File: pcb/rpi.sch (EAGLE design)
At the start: 32 parts, among them IC1 LD117AS33TR, SW1 324_SW, SW20 324_SW, U5 CH340C

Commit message: rpi carrier board finished
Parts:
- removed C14, C15, C17, C19, C35: 100nF, clock:CAP0805
- removed C18: 1uF, clock:CAP0805
- removed U$2, U$3, U$4, U$5: M2.5HOLE, f1c100s:M2.5HOLE
- added JP3, JP4, JP5: (no value), pinhead:PINHD-1X3
- added R2, R3: 390K, SparkFun-Passives:RESISTOR0805-RES
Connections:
- removed net N$17: SW20.2, SW20.3
- removed net N$4: SW1.2, SW1.3
- new net N$11: JP1.15, JP2.15, PCB1.GPIO22, R3.1, SW20.2, SW20.3
- new net N$12: JP1.19, JP2.19, PCB1.GPIO10, U2.SDIN
- new net N$13: JP1.21, JP2.21, PCB1.GPIO9
- new net N$14: JP1.23, JP2.23, PCB1.GPIO11, U2.SCLK
- new net N$15: JP1.27, JP2.27, PCB1.ID_SD*
- new net N$16: JP1.29, JP2.29, PCB1.GPIO5, U2.DC
- new net N$19: JP1.33, JP2.33, PCB1.GPIO13
- new net N$20: JP1.35, JP2.35, PCB1.GPIO19
- new net N$21: JP1.37, JP2.37, PCB1.GPIO26
- new net N$22: JP1.12, JP2.12, PCB1.GPIO18
- new net N$23: JP1.16, JP2.16, PCB1.GPIO23
- new net N$24: JP1.18, JP2.18, PCB1.GPIO24
- new net N$25: JP1.22, JP2.22, PCB1.GPIO25
- new net N$26: JP1.24, JP2.24, PCB1.GPIO8
- new net N$27: JP1.26, JP2.26, PCB1.GPIO7, U2./CS
- new net N$28: JP1.28, JP2.28, PCB1.ID_SC*
- new net N$29: JP1.32, JP2.32, PCB1.GPIO12
- new net N$30: JP1.36, JP2.36, PCB1.GPIO16
- new net N$31: JP1.38, JP2.38, PCB1.GPIO20
- new net N$32: JP1.40, JP2.40, PCB1.GPIO21
- new net N$34: JP1.13, JP2.13, PCB1.GPIO27, R2.1, SW1.2, SW1.3
- new net N$5: JP1.3, JP2.3, PCB1.GPIO2
- new net N$6: JP1.5, JP2.5, PCB1.GPIO3
- new net N$8: JP1.7, JP2.7, PCB1.GPIO4
- new net N$9: JP1.11, JP2.11, PCB1.GPIO17
- net +3V3: now also JP2.17, JP3.1, JP3.2, JP3.3, R2.2, R3.2; no longer C14.2, C15.2, C17.2, C18.2, C19.2, C35.2
- net +5V: now also JP5.1, JP5.2, JP5.3
- net GND: now also JP4.1, JP4.2, JP4.3; no longer C14.1, C15.1, C17.1, C18.1, C19.1, C35.1
- net N$43: now also JP1.31, JP2.31, PCB1.GPIO6
- net UART0_RX: now also JP1.10, JP2.10
- net UART0_TX: now also JP1.8, JP2.8
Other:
- moved on the sheet: C20, C21, C22, C23, JP1, R7, R8, U2

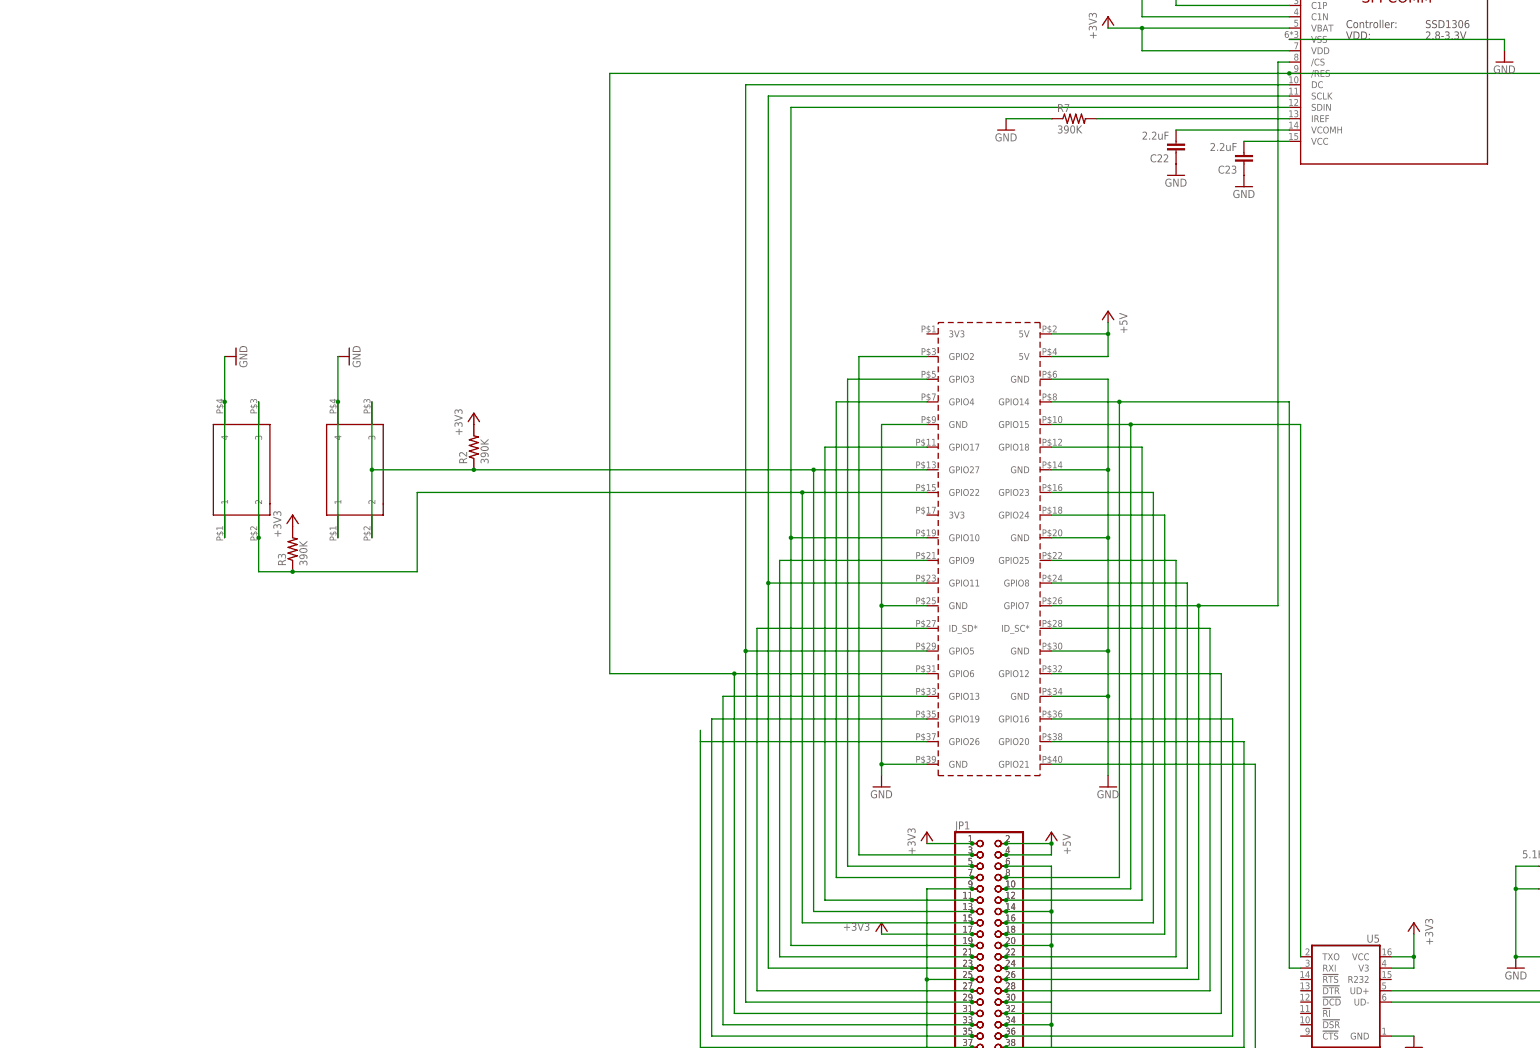
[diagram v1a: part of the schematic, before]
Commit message: updated baseboard, added power buttons
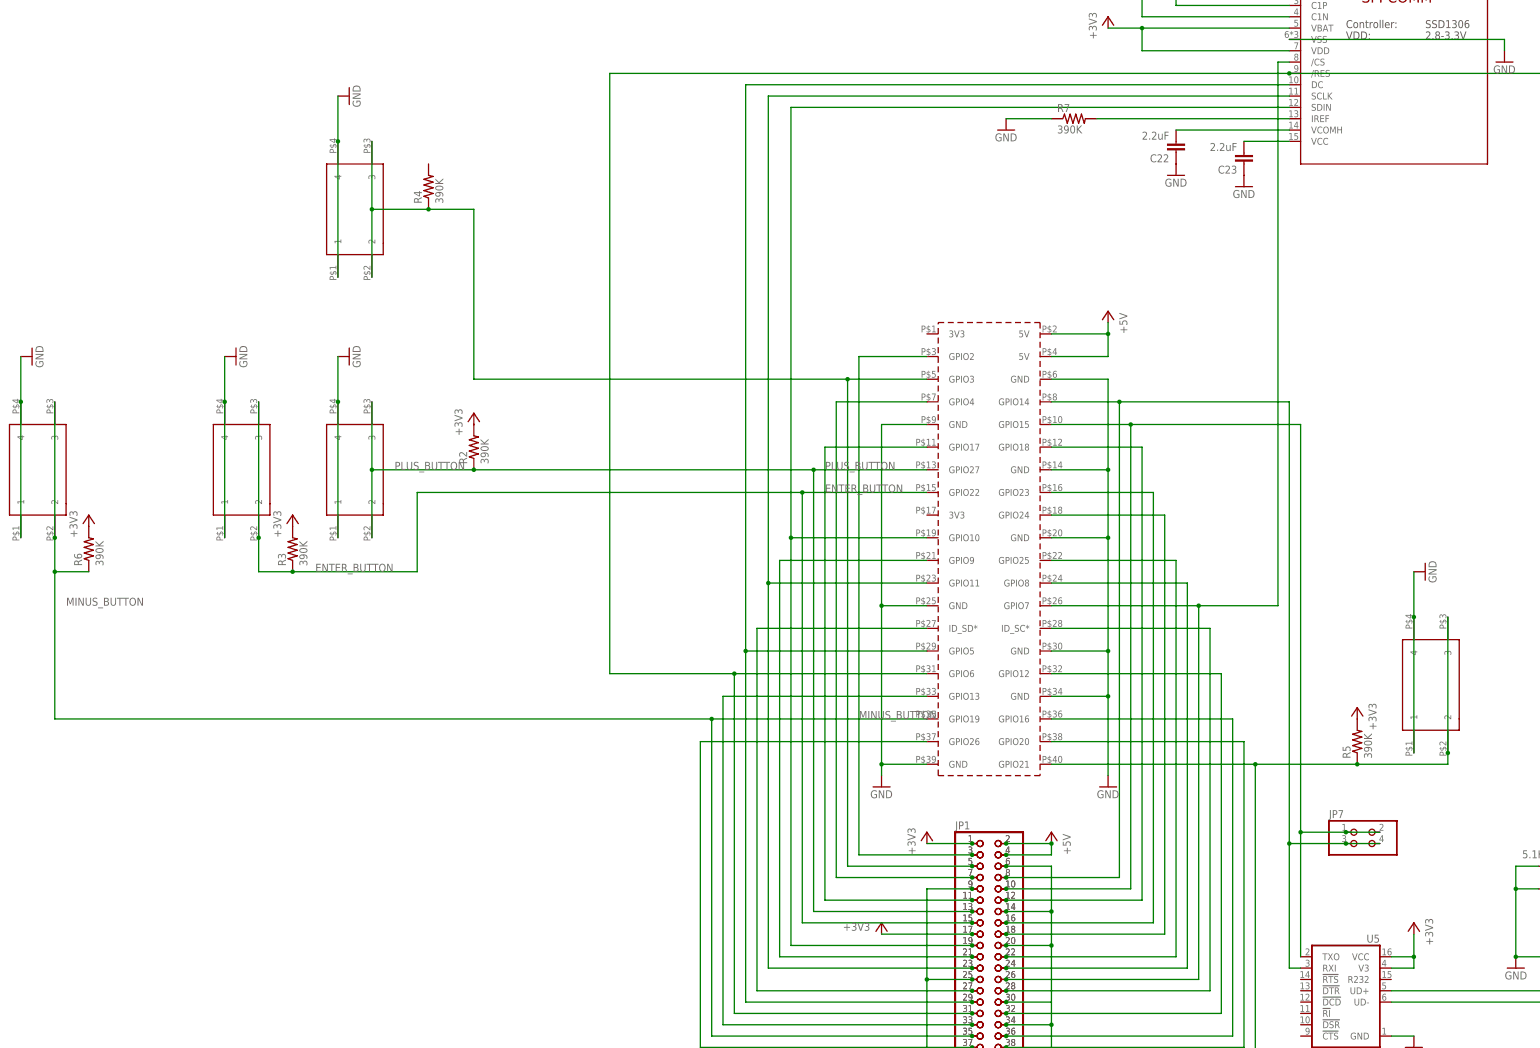
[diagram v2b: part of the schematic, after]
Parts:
- added JP7: (no value), pinhead:PINHD-2X2
- added R4, R5, R6: 390K, SparkFun-Passives:RESISTOR0805-RES
- added SW2, SW3, SW4: 324_SW, 3pos_slide_switch_centered:324_SW
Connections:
- net N$11 renamed ENTER_BUTTON
- net N$34 renamed PLUS_BUTTON
- removed net N$20: JP1.35, JP2.35, PCB1.GPIO19
- removed net UART0_RX: JP1.10, JP2.10, PCB1.GPIO15, U5.TXO
- removed net UART0_TX: JP1.8, JP2.8, PCB1.GPIO14, U5.RXI
- new net MINUS_BUTTON: JP1.35, JP2.35, PCB1.GPIO19, R6.1, SW4.2, SW4.3
- new net RPI_RX: JP1.10, JP2.10, JP7.1, JP7.2, PCB1.GPIO15, U5.TXO
- new net RPI_TX: JP1.8, JP2.8, JP7.3, JP7.4, PCB1.GPIO14, U5.RXI
- net +3V3: now also R5.2, R6.2
- net GND: now also SW2.1, SW2.4, SW3.1, SW3.4, SW4.1, SW4.4
- net N$32: now also R5.1, SW3.2, SW3.3
- net N$6: now also R4.1, SW2.2, SW2.3

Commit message: added i2c pullups, cleanup
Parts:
- removed R4: 390K, SparkFun-Passives:RESISTOR0805-RES
- added R10, R11: 5.1K, joyAnalog:RESISTOR0805-RES
- added U$2, U$3: M2.5HOLE, f1c100s:M2.5HOLE
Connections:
- net +3V3: now also R10.1, R11.1
- net N$5: now also R11.2
- net N$6: now also R10.2; no longer R4.1
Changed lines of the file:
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@@
 <layer number="250" name="Descript" color="3" fill="1" visible="no" active="no"/>
 <layer number="251" name="SMDround" color="12" fill="11" visible="no" active="no"/>
+<layer number="253" name="Extra" color="7" fill="1" visible="no" active="no"/>
 <layer number="254" name="cooling" color="7" fill="1" visible="yes" active="yes"/>
 <layer number="255" name="routoute" color="7" fill="1" visible="yes" active="yes"/>
@@
 <part name="SW3" library="3pos_slide_switch_centered" deviceset="324_SW" device="" value="324_SW"/>
 <part name="GND9" library="supply1" library_urn="urn:adsk.eagle:library:371" deviceset="GND" device=""/>
-<part name="R4" library="SparkFun-Passives" deviceset="RESISTOR" device="0805-RES" value="390K"/>
 <part name="R5" library="SparkFun-Passives" deviceset="RESISTOR" device="0805-RES" value="390K"/>
 <part name="+3V7" library="supply1" library_urn="urn:adsk.eagle:library:371" deviceset="+3V3" device=""/>
@@
 <part name="R6" library="SparkFun-Passives" deviceset="RESISTOR" device="0805-RES" value="390K"/>
 <part name="+3V8" library="supply1" library_urn="urn:adsk.eagle:library:371" deviceset="+3V3" device=""/>
+<part name="R10" library="joyAnalog" deviceset="RESISTOR" device="0805-RES" value="5.1K"/>
+<part name="R11" library="joyAnalog" deviceset="RESISTOR" device="0805-RES" value="5.1K"/>
+<part name="+3V9" library="supply1" library_urn="urn:adsk.eagle:library:371" deviceset="+3V3" device=""/>
+<part name="+3V12" library="supply1" library_urn="urn:adsk.eagle:library:371" deviceset="+3V3" device=""/>
+<part name="U$2" library="f1c100s" deviceset="M2.5HOLE" device=""/>
+<part name="U$3" library="f1c100s" deviceset="M2.5HOLE" device=""/>
 </parts>
 <sheets>
@@
 <attribute name="VALUE" x="739.14" y="40.64" size="1.778" layer="96" rot="R90"/>
 </instance>
-<instance part="R4" gate="G$1" x="513.08" y="129.54" smashed="yes" rot="R90">
-<attribute name="NAME" x="511.5814" y="125.73" size="1.778" layer="95" rot="R90"/>
-<attribute name="VALUE" x="516.382" y="125.73" size="1.778" layer="96" rot="R90"/>
-</instance>
 <instance part="R5" gate="G$1" x="721.36" y="5.08" smashed="yes" rot="R90">
 <attribute name="NAME" x="719.8614" y="1.27" size="1.778" layer="95" rot="R90"/>
@@
 <attribute name="VALUE" x="434.34" y="50.8" size="1.778" layer="96" rot="R90"/>
 </instance>
+<instance part="R10" gate="G$1" x="645.16" y="111.76" smashed="yes" rot="MR270">
+<attribute name="NAME" x="643.6614" y="113.03" size="1.778" layer="95" rot="MR270"/>
+<attribute name="VALUE" x="643.382" y="107.95" size="1.778" layer="96" rot="MR270"/>
+</instance>
+<instance part="R11" gate="G$1" x="632.46" y="111.76" smashed="yes" rot="MR270">
+<attribute name="NAME" x="630.9614" y="113.03" size="1.778" layer="95" rot="MR270"/>
+<attribute name="VALUE" x="630.682" y="107.95" size="1.778" layer="96" rot="MR270"/>
+</instance>
+<instance part="+3V9" gate="G$1" x="645.16" y="124.46" smashed="yes">
+<attribute name="VALUE" x="642.62" y="119.38" size="1.778" layer="96" rot="R90"/>
+</instance>
+<instance part="+3V12" gate="G$1" x="632.46" y="124.46" smashed="yes">
+<attribute name="VALUE" x="629.92" y="119.38" size="1.778" layer="96" rot="R90"/>
+</instance>
+<instance part="U$2" gate="G$1" x="881.38" y="88.9" smashed="yes"/>
+<instance part="U$3" gate="G$1" x="881.38" y="73.66" smashed="yes"/>
 </instances>
 <busses>
@@
 <pinref part="+3V8" gate="G$1" pin="+3V3"/>
 </segment>
+<segment>
+<pinref part="R10" gate="G$1" pin="1"/>
+<pinref part="+3V9" gate="G$1" pin="+3V3"/>
+<wire x1="645.16" y1="121.92" x2="645.16" y2="116.84" width="0.1524" layer="91"/>
+</segment>
+<segment>
+<pinref part="R11" gate="G$1" pin="1"/>
+<pinref part="+3V12" gate="G$1" pin="+3V3"/>
+<wire x1="632.46" y1="121.92" x2="632.46" y2="116.84" width="0.1524" layer="91"/>
+</segment>
 </net>
 <net name="N$2" class="0">
@@
 <pinref part="JP2" gate="A" pin="3"/>
 <junction x="635" y="-20.32"/>
+<pinref part="R11" gate="G$1" pin="2"/>
+<wire x1="632.46" y1="106.68" x2="632.46" y2="91.44" width="0.1524" layer="91"/>
+<wire x1="632.46" y1="91.44" x2="624.84" y2="91.44" width="0.1524" layer="91"/>
+<junction x="624.84" y="91.44"/>
 </segment>
 </net>
@@
 <wire x1="500.38" y1="124.46" x2="500.38" y2="139.7" width="0.1524" layer="91"/>
 <junction x="500.38" y="124.46"/>
-<wire x1="523.24" y1="124.46" x2="513.08" y2="124.46" width="0.1524" layer="91"/>
-<wire x1="513.08" y1="124.46" x2="500.38" y2="124.46" width="0.1524" layer="91"/>
+<wire x1="523.24" y1="124.46" x2="500.38" y2="124.46" width="0.1524" layer="91"/>
 <wire x1="607.06" y1="86.36" x2="523.24" y2="86.36" width="0.1524" layer="91"/>
 <wire x1="523.24" y1="86.36" x2="523.24" y2="124.46" width="0.1524" layer="91"/>
 <junction x="607.06" y="86.36"/>
-<pinref part="R4" gate="G$1" pin="1"/>
-<junction x="513.08" y="124.46"/>
-</segment>
-</net>
+<pinref part="R10" gate="G$1" pin="2"/>
+<wire x1="645.16" y1="106.68" x2="645.16" y2="86.36" width="0.1524" layer="91"/>
+<wire x1="645.16" y1="86.36" x2="624.84" y2="86.36" width="0.1524" layer="91"/>
+<junction x="624.84" y="86.36"/>
+</segment>
+</net>

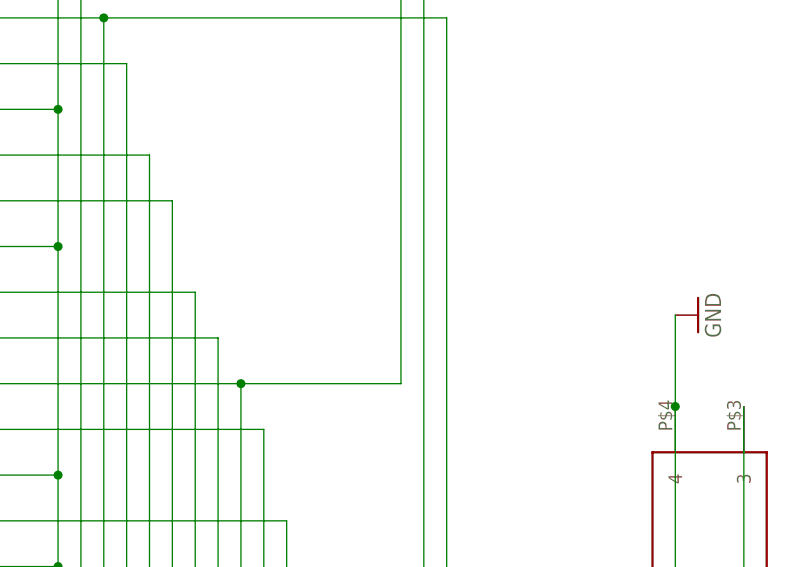
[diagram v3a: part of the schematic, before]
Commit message: finished ADB protocol board
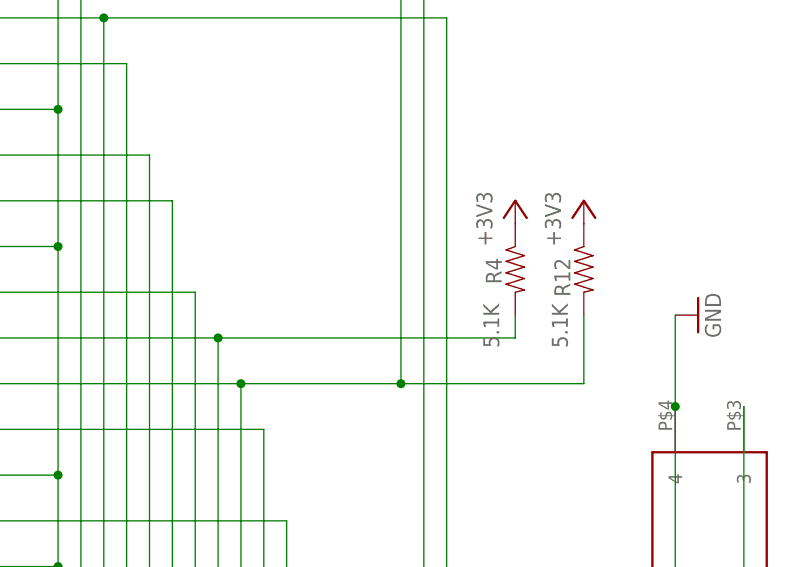
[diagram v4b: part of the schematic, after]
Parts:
- added R12, R4: 5.1K, joyAnalog:RESISTOR0805-RES
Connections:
- net +3V3: now also R12.1, R4.1
- net N$26: now also R4.2
- net N$27: now also R12.2
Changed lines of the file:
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@@
 <part name="U$2" library="f1c100s" deviceset="M2.5HOLE" device=""/>
 <part name="U$3" library="f1c100s" deviceset="M2.5HOLE" device=""/>
+<part name="R4" library="joyAnalog" deviceset="RESISTOR" device="0805-RES" value="5.1K"/>
+<part name="R12" library="joyAnalog" deviceset="RESISTOR" device="0805-RES" value="5.1K"/>
+<part name="+3V13" library="supply1" library_urn="urn:adsk.eagle:library:371" deviceset="+3V3" device=""/>
+<part name="+3V15" library="supply1" library_urn="urn:adsk.eagle:library:371" deviceset="+3V3" device=""/>
 </parts>
 <sheets>
@@
 <instance part="U$2" gate="G$1" x="881.38" y="88.9" smashed="yes"/>
 <instance part="U$3" gate="G$1" x="881.38" y="73.66" smashed="yes"/>
+<instance part="R4" gate="G$1" x="716.28" y="48.26" smashed="yes" rot="MR270">
+<attribute name="NAME" x="714.7814" y="49.53" size="1.778" layer="95" rot="MR270"/>
+<attribute name="VALUE" x="714.502" y="44.45" size="1.778" layer="96" rot="MR270"/>
+</instance>
+<instance part="R12" gate="G$1" x="723.9" y="48.26" smashed="yes" rot="MR270">
+<attribute name="NAME" x="722.4014" y="49.53" size="1.778" layer="95" rot="MR270"/>
+<attribute name="VALUE" x="722.122" y="44.45" size="1.778" layer="96" rot="MR270"/>
+</instance>
+<instance part="+3V13" gate="G$1" x="723.9" y="55.88" smashed="yes">
+<attribute name="VALUE" x="721.36" y="50.8" size="1.778" layer="96" rot="R90"/>
+</instance>
+<instance part="+3V15" gate="G$1" x="716.28" y="55.88" smashed="yes">
+<attribute name="VALUE" x="713.74" y="50.8" size="1.778" layer="96" rot="R90"/>
+</instance>
 </instances>
 <busses>
@@
 <wire x1="632.46" y1="121.92" x2="632.46" y2="116.84" width="0.1524" layer="91"/>
 </segment>
+<segment>
+<pinref part="R12" gate="G$1" pin="1"/>
+<pinref part="+3V13" gate="G$1" pin="+3V3"/>
+</segment>
+<segment>
+<pinref part="R4" gate="G$1" pin="1"/>
+<pinref part="+3V15" gate="G$1" pin="+3V3"/>
+</segment>
 </net>
 <net name="N$2" class="0">
@@
 <pinref part="JP2" gate="A" pin="24"/>
 <junction x="642.62" y="-45.72"/>
+<pinref part="R4" gate="G$1" pin="2"/>
+<wire x1="683.26" y1="40.64" x2="716.28" y2="40.64" width="0.1524" layer="91"/>
+<wire x1="716.28" y1="40.64" x2="716.28" y2="43.18" width="0.1524" layer="91"/>
+<junction x="683.26" y="40.64"/>
 </segment>
 </net>
@@
 <wire x1="703.58" y1="35.56" x2="685.8" y2="35.56" width="0.1524" layer="91"/>
 <junction x="685.8" y="35.56"/>
-</segment>
-</net>
+<pinref part="R12" gate="G$1" pin="2"/>
+<wire x1="703.58" y1="35.56" x2="723.9" y2="35.56" width="0.1524" layer="91"/>
+<wire x1="723.9" y1="35.56" x2="723.9" y2="43.18" width="0.1524" layer="91"/>
+<junction x="703.58" y="35.56"/>
+</segment>
+</net>
